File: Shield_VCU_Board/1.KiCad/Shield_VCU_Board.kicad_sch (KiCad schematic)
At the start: 162 parts, among them J1 Conn_02x08_Odd_Even, J10 Main_Supply, J11 Conn_01x40_Socket, J12 TFT Wire, J13 Conn_Molex_TouchPanel, J14 CAN_OUT, J15 Conn_01x04_Socket, J16 CAN_IN, J2 Conn_02x10_Odd_Even, J3/1 NXP3, J4 Conn_02x08_Odd_Even, J5 Conn_02x10_Odd_Even, J6 Conn_02x10_Odd_Even, J7 Button_Activation_Logic, J8 Conn_ToSpeaker, J9 Wire_x06_Pin, Q1 BSS138, Q2 BSS138, Q3 BSS138, Q4 BSS138, U1 AS1115-BSST, U10 TPS61165-Q1, U13 TPS54202DDC, U2 SN74LVC1G125DBV, U3 MC74HC14A, U4 TPA6211A1 - ?, U7 FT813Q, U8 TLV76133DCY, U9 TLV76133DCY

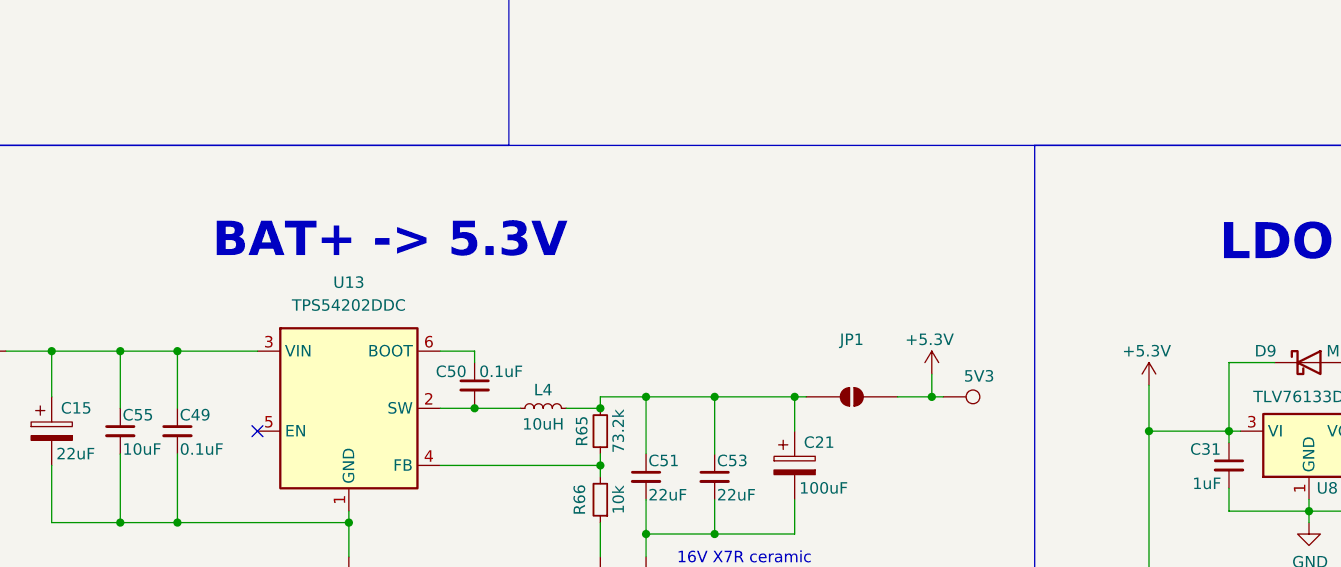
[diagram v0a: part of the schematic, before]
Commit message: 3Dmodel_v2.2 - added
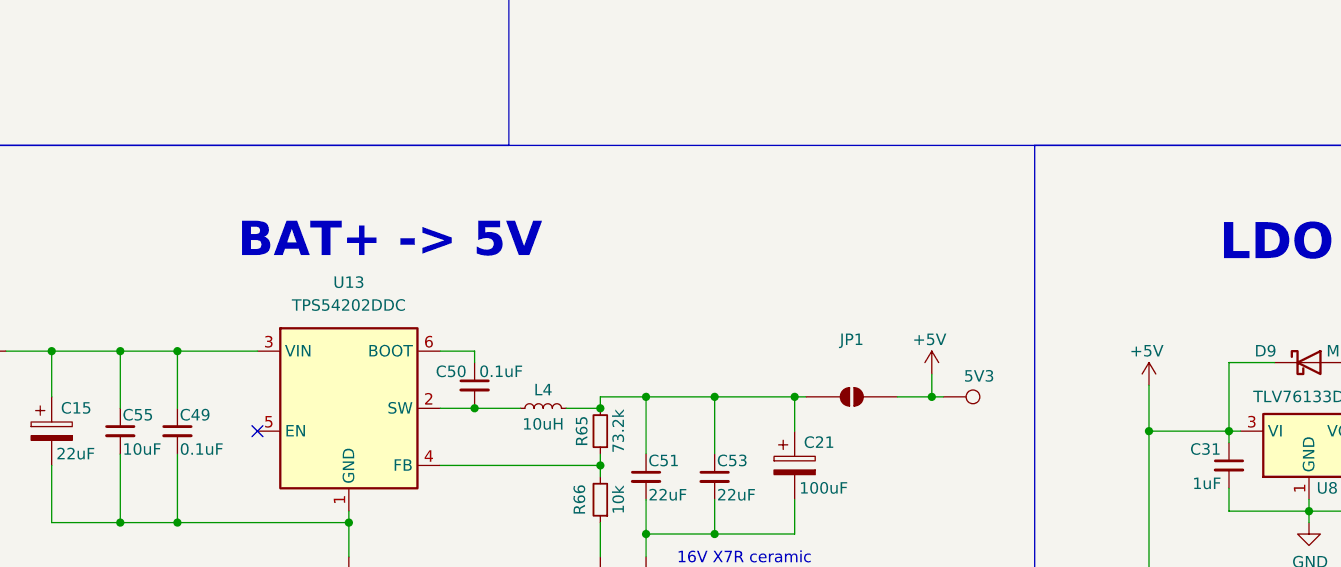
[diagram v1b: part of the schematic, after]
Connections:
- net +5.3V: no longer 5V3.1, C31.1, C33.1, D10.1 (K), D9.1 (K), JP1.2 (B), U8.3 (VI), U9.3 (VI)
- new net +5V: 5V3.1, C31.1, C33.1, D10.1 (K), D9.1 (K), JP1.2 (B), U8.3 (VI), U9.3 (VI)
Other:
- note added: "BAT+ -> 5V"
- note removed: "BAT+ -> 5.3V"
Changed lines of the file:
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@@
 		)
 	)
-	(text "BAT+ -> 5.3V"
+	(text "BAT+ -> 5V"
 		(exclude_from_sim no)
 		(at 75.692 229.108 0)
@@
 			)
 		)
-		(property "Value" "+5.3V"
+		(property "Value" "+5V"
 			(at 135.636 240.03 0)
 			(show_name no)
@@
 	)
 	(symbol
-		(lib_id "power:+5V")
-		(at 160.02 245.11 0)
-		(unit 1)
-		(body_style 1)
-		(exclude_from_sim no)
-		(in_bom yes)
-		(on_board yes)
-		(in_pos_files yes)
-		(dnp no)
-		(property "Reference" "#PWR084"
-			(at 160.02 248.92 0)
-			(hide yes)
-			(show_name no)
-			(do_not_autoplace no)
-			(effects
-				(font
-					(size 1.27 1.27)
-				)
-			)
-		)
-		(property "Value" "+5.3V"
-			(at 159.766 241.3 0)
-			(show_name no)
-			(do_not_autoplace no)
-			(effects
-				(font
-					(size 1.27 1.27)
-				)
-			)
-		)
-		(property "Footprint" ""
-			(at 160.02 245.11 0)
-			(hide yes)
-			(show_name no)
-			(do_not_autoplace no)
-			(effects
-				(font
-					(size 1.27 1.27)
-				)
-			)
-		)
-		(property "Datasheet" ""
-			(at 160.02 245.11 0)
-			(hide yes)
-			(show_name no)
-			(do_not_autoplace no)
-			(effects
-				(font
-					(size 1.27 1.27)
-				)
-			)
-		)
-		(property "Description" ""
-			(at 160.02 245.11 0)
-			(show_name no)
-			(do_not_autoplace no)
-			(effects
-				(font
-					(size 1.27 1.27)
-				)
-			)
-		)
-		(pin "1"
-		)
-		(instances
-			(project "Shield_VCU_Board"
-				(path "/4a8cb20d-5f30-4163-a2c8-18e2deeb65d3"
-					(reference "#PWR084")
-					(unit 1)
-				)
-			)
-		)
-	)
-	(symbol
 		(lib_id "power:+3V3")
 		(at 170.18 312.42 0)
@@
 					(unit 1)
 				)
+			)
+		)
+	)
+	(symbol
+		(lib_id "power:+5V")
+		(at 160.02 245.11 0)
+		(unit 1)
+		(body_style 1)
+		(exclude_from_sim no)
+		(in_bom yes)
+		(on_board yes)
+		(in_pos_files yes)
+		(dnp no)
+		(property "Reference" "#PWR082"
+			(at 160.02 248.92 0)
+			(hide yes)
+			(show_name no)
+			(do_not_autoplace no)
+			(effects
+				(font
+					(size 1.27 1.27)
+				)
+			)
+		)
+		(property "Value" "+5V"
+			(at 159.766 241.3 0)
+			(show_name no)
+			(do_not_autoplace no)
+			(effects
+				(font
+					(size 1.27 1.27)
+				)
+			)
+		)
+		(property "Footprint" ""
+			(at 160.02 245.11 0)
+			(hide yes)
+			(show_name no)
+			(do_not_autoplace no)
+			(effects
+				(font
+					(size 1.27 1.27)
+				)
+			)
+		)
+		(property "Datasheet" ""
+			(at 160.02 245.11 0)
+			(hide yes)
+			(show_name no)
+			(do_not_autoplace no)
+			(effects
+				(font
+					(size 1.27 1.27)
+				)
+			)
+		)
+		(property "Description" ""
+			(at 160.02 245.11 0)
+			(show_name no)
+			(do_not_autoplace no)
+			(effects
+				(font
+					(size 1.27 1.27)
+				)
+			)
+		)
+		(pin "1"
+		)
+		(instances
+			(project "Shield_VCU_Board"
+				(path "/4a8cb20d-5f30-4163-a2c8-18e2deeb65d3"
+					(reference "#PWR082")
+					(unit 1)
+				)

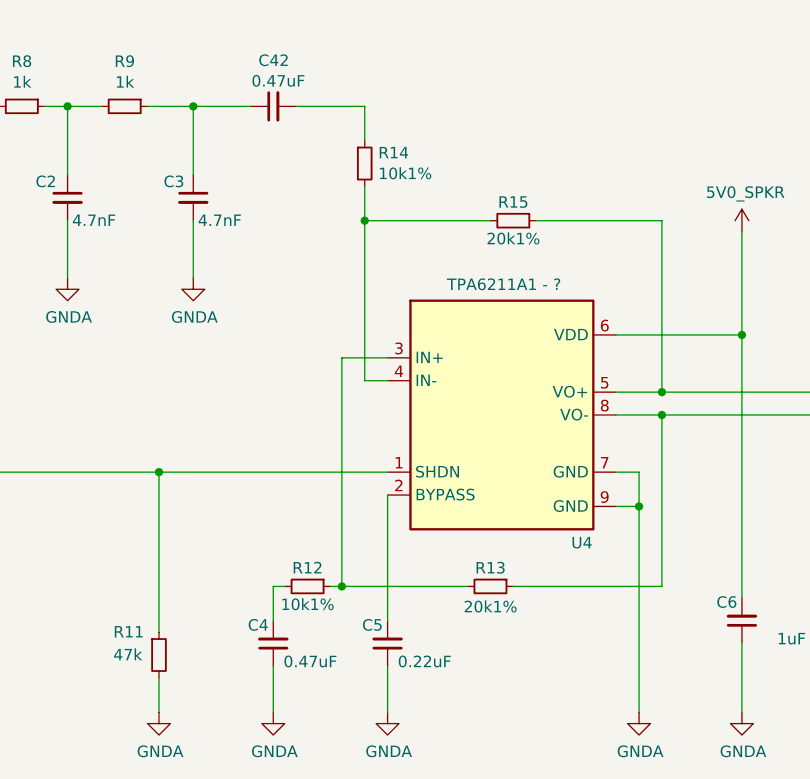
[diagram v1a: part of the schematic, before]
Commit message: Updated resistors for audio
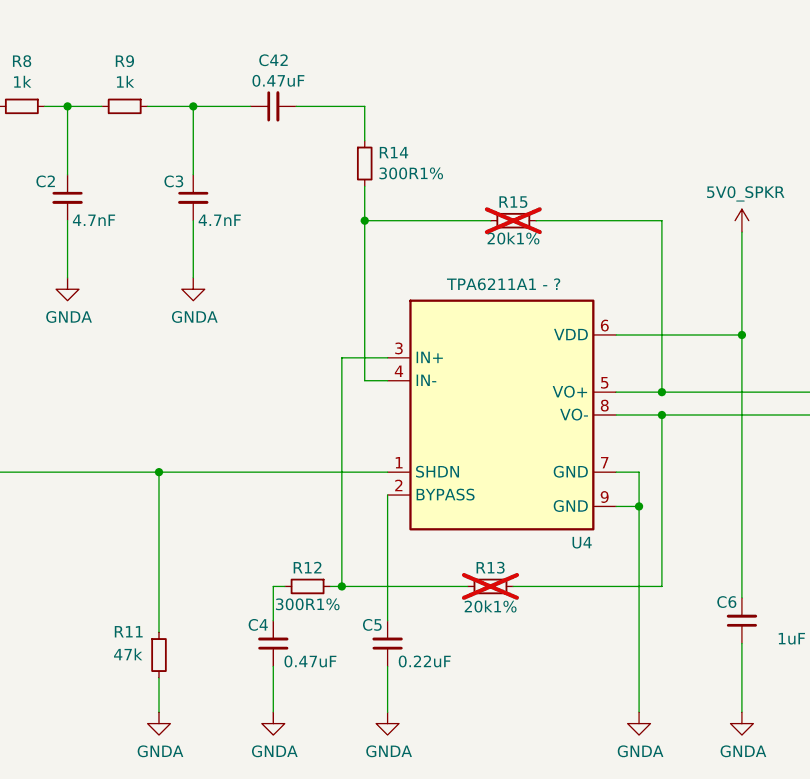
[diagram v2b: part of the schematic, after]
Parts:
- R12, R14: value 10k1% -> 300R1%
- R13, R15: now not fitted
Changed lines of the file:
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@@
 		(on_board yes)
 		(in_pos_files yes)
-		(dnp no)
+		(dnp yes)
 		(property "Reference" "R15"
 			(at 513.08 304.038 90)
@@
 			)
 		)
-		(property "Value" "10k1%"
+		(property "Value" "300R1%"
 			(at 498.0686 300.863 0)
 			(show_name no)
@@
 			)
 		)
-		(property "Value" "10k1%"
+		(property "Value" "300R1%"
 			(at 490.22 348.742 90)
 			(show_name no)
@@
 		(on_board yes)
 		(in_pos_files yes)
-		(dnp no)
+		(dnp yes)
 		(property "Reference" "R13"
 			(at 510.54 344.678 90)

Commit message: Corrections on TouchScreen pin RST & INT swap
*Additional: 33R resistor footprint change to match real part
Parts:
- L4: value 10uH -> 15uF
- RN8: footprint Resistor_SMD:R_Cat16-4 -> Resistor_SMD:R_Array_Convex_4x0402
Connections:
- net +5.3V is gone; now on net +5V: C38.1, FB2.1, JP3.2 (B), L2.1, R19.2
- net at J13.5 (Pin_5): now also RN8.2 (R2.1); no longer RN8.1 (R1.1)
- net at J13.6 (Pin_6): now also RN8.1 (R1.1); no longer RN8.2 (R2.1)
